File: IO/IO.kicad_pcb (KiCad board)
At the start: 2 copper layers, 100 x 100 mm, 36 parts, among them J1 Parallel, J2 Serial, J3 Buss, SW1 Slot, U1 74LS123, U2 74LS85, U3 MC6850, U4 MC6821, U5 74LS393, U6 74LS10, U7 74LS139, Y1 1.8432MHz

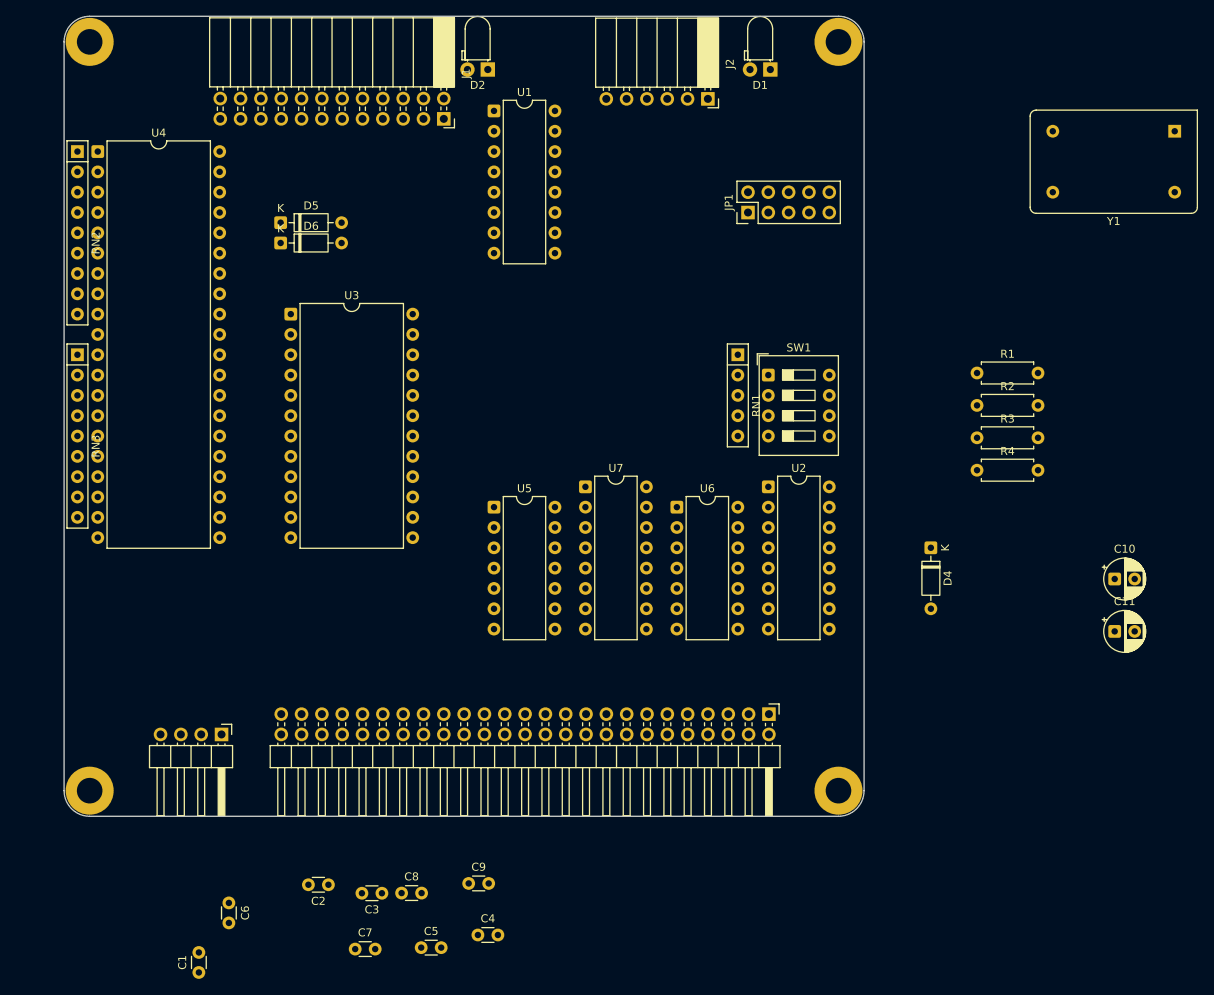
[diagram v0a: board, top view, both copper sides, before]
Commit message: finish routing the coms board. add some step models to look at this thing in freecad
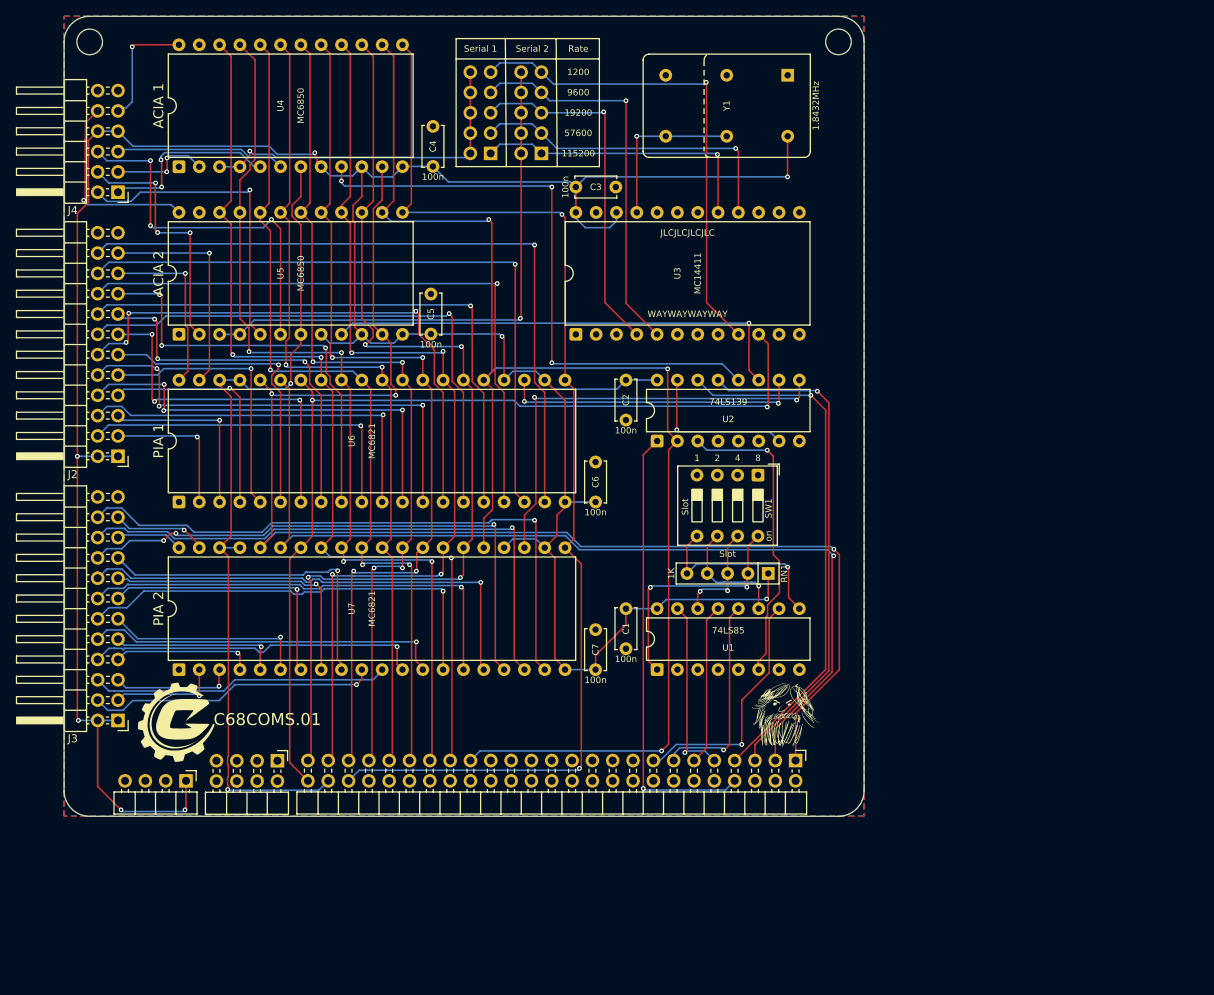
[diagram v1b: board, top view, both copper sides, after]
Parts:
- removed the C1 at (41.8, 144.5)
- removed C10, C11: 1µF, Capacitor_THT:CP_Radial_D5.0mm_P2.50mm
- removed C9: 100n, Capacitor_THT:C_Disc_D3.0mm_W1.6mm_P2.50mm
- removed D1: ACIA, LED_THT:LED_D3.0mm_Horizontal_O1.27mm_Z2.0mm
- removed D2: PIA, LED_THT:LED_D3.0mm_Horizontal_O1.27mm_Z2.0mm
- removed D4, D5, D6: 1N4148, Diode_THT:D_DO-35_SOD27_P7.62mm_Horizontal
- removed the J2 at (105.5, 35.3)
- removed R1, R2: 1K, Resistor_THT:R_Axial_DIN0207_L6.3mm_D2.5mm_P7.62mm_Horizontal
- removed R3, R4: 100K, Resistor_THT:R_Axial_DIN0207_L6.3mm_D2.5mm_P7.62mm_Horizontal
- removed RN2, RN3: 4.7K, Resistor_THT:R_Array_SIP9
- removed the U1 at (78.7, 36.8)
- removed the U6 at (101.6, 86.4)
- added G1: Logo, 0-Footprints:Crank, F.Cu at (39.1, 113.3)
- added G2: Logo, 0-Footprints:crankery_small, F.Cu at (114.9, 112.4)
- added J3: PIA 2, Connector_PinHeader_2.54mm:PinHeader_2x12_P2.54mm_Horizontal, F.Cu at (31.7, 113.0)
- added J4: Serial, Connector_PinHeader_2.54mm:PinHeader_2x06_P2.54mm_Horizontal, F.Cu at (31.7, 47.0)
- added JP2: RATE_{2}, 0-Footprints:PinHeader_2x05_P2.54mm_Vertical, F.Cu at (84.7, 42.1)
- added U3: MC14411, 0-Footprints:DIP-24_W15.24mm, F.Cu at (89.0, 64.8)
- added U7: MC6821, 0-Footprints:DIP-40_W15.24mm, F.Cu at (39.4, 106.7)
- C1: renamed from C2; footprint Capacitor_THT:C_Disc_D3.0mm_W1.6mm_P2.50mm -> 0-Footprints:C_Disc_D5.0mm_W2.5mm_P5.00mm
- C2: renamed from C7; footprint Capacitor_THT:C_Disc_D3.0mm_W1.6mm_P2.50mm -> 0-Footprints:C_Disc_D5.0mm_W2.5mm_P5.00mm
- C3, C4, C5, C6: footprint Capacitor_THT:C_Disc_D3.0mm_W1.6mm_P2.50mm -> 0-Footprints:C_Disc_D5.0mm_W2.5mm_P5.00mm
- C7: renamed from C8; footprint Capacitor_THT:C_Disc_D3.0mm_W1.6mm_P2.50mm -> 0-Footprints:C_Disc_D5.0mm_W2.5mm_P5.00mm
- J2: renamed from J1; value Parallel -> PIA 1; footprint Connector_PinSocket_2.54mm:PinSocket_2x12_P2.54mm_Horizontal -> Connector_PinHeader_2.54mm:PinHeader_2x12_P2.54mm_Horizontal
- JP1: value SERCLKx16 -> RATE_{1}; footprint Connector_PinHeader_2.54mm:PinHeader_2x05_P2.54mm_Vertical -> 0-Footprints:PinHeader_2x05_P2.54mm_Vertical
- RN1: footprint Resistor_THT:R_Array_SIP5 -> 0-Footprints:R_Array_SIP5
- SW1: footprint Button_Switch_THT:SW_DIP_SPSTx04_Slide_9.78x12.34mm_W7.62mm_P2.54mm -> 0-Footprints:SW_DIP_SPSTx04_Slide_9.78x12.34mm_W7.62mm_P2.54mm
- U1: renamed from U2; footprint Package_DIP:DIP-16_W7.62mm -> 0-Footprints:DIP-16_W7.62mm
- U2: renamed from U7; footprint Package_DIP:DIP-16_W7.62mm -> 0-Footprints:DIP-16_W7.62mm
- U4: renamed from U3; footprint Package_DIP:DIP-24_W15.24mm -> 0-Footprints:DIP-24_W15.24mm
- U5: value 74LS393 -> MC6850; footprint Package_DIP:DIP-14_W7.62mm -> 0-Footprints:DIP-24_W15.24mm
- U6: renamed from U4; footprint Package_DIP:DIP-40_W15.24mm -> 0-Footprints:DIP-40_W15.24mm
- Y1: footprint Oscillator:Oscillator_DIP-14 -> 0-Footprints:Oscillator_DIP-14
- moved C4 101.2 mm to (71.1, 38.8), turned to -90 degrees
- moved C3 93.0 mm to (94.0, 46.3)
- moved C5 81.7 mm to (70.9, 59.7), turned to -90 degrees
- moved C2 78.8 mm to (95.2, 70.5), turned to -90 degrees
- moved C6 71.7 mm to (91.4, 80.7)
- moved J2 58.6 mm to (31.7, 80.0), turned to 180 degrees
- moved C1 50.7 mm to (95.2, 99.0), turned to -90 degrees
- moved Y1 48.9 mm to (115.5, 32.4)
- moved U6 45.0 mm to (39.4, 85.7), turned to 90 degrees
- moved U5 44.9 mm to (39.4, 64.8), turned to 90 degrees
- moved C7 40.9 mm to (91.4, 101.7), turned to -90 degrees
- moved JP1 33.0 mm to (78.3, 42.1), turned to 180 degrees
- moved RN1 27.6 mm to (113.0, 94.7), turned to 180 degrees
- moved U1 26.7 mm to (99.1, 106.7), turned to 90 degrees
- moved U4 23.1 mm to (39.4, 43.8), turned to 90 degrees
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- renumbered J3 to J1
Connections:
- net Net-(J1-Pin_10) renamed /PB3
- net Net-(J1-Pin_11) renamed /PA4
- net Net-(J1-Pin_12) renamed /PB4
- net Net-(J1-Pin_13) renamed /PA5
- net Net-(J1-Pin_14) renamed /PB5
- net Net-(J1-Pin_15) renamed /PA6
- net Net-(J1-Pin_16) renamed /PB6
- net Net-(J1-Pin_17) renamed /PA7
- net Net-(J1-Pin_18) renamed /PB7
- net Net-(J1-Pin_19) renamed /CA1
- net Net-(J1-Pin_20) renamed /CB1
- net Net-(J1-Pin_21) renamed /CA2
- net Net-(J1-Pin_22) renamed /CB2
- net Net-(J1-Pin_3) renamed /PA0
- net Net-(J1-Pin_4) renamed /PB0
- net Net-(J1-Pin_5) renamed /PA1
- net Net-(J1-Pin_6) renamed /PB1
- net Net-(J1-Pin_7) renamed /PA2
- net Net-(J1-Pin_8) renamed /PB2
- net Net-(J1-Pin_9) renamed /PA3
- C3 pad 1: +5V -> GND
- C3 pad 2: GND -> +5V
- C4 pad 1: +5V -> GND
- C4 pad 2: GND -> +5V
- C5 pad 1: +5V -> GND
- C5 pad 2: GND -> +5V
- C6 pad 1: +5V -> GND
- C6 pad 2: GND -> +5V
- C7 pad 1: +5V -> GND
- C7 pad 2: GND -> +5V
- J1 pad 19: A9 -> unconnected-(J1-A_{9}-Pad19)
- J1 pad 21: A10 -> unconnected-(J1-A_{10}-Pad21)
- J1 pad 23: A11 -> unconnected-(J1-A_{11}-Pad23)
- J1 pad 25: A12 -> unconnected-(J1-A_{12}-Pad25)
- J1 pad 27: A13 -> unconnected-(J1-A_{13}-Pad27)
- J1 pad 29: A14 -> unconnected-(J1-A_{14}-Pad29)
- J1 pad 31: A15 -> unconnected-(J1-A_{15}-Pad31)
- J1 pad 48: Net-(D4-A) -> ~{IRQ}
- JP1 pad 1: /115200 -> 115.2Kbps
- JP1 pad 3: /57600 -> 57.6Kbps
- JP1 pad 5: /19200 -> 19.2Kbps
- JP1 pad 7: /9600 -> 9.6Kbps
- JP1 pad 9: /1200 -> 1.2Kbps
- U1 pad 6: Net-(U2-Oa=b) -> SLOT_SEL
- U2 pad 1: Net-(U7A-E) -> ~{IO_SEL}
- U2 pad 10: unconnected-(U7B-O2-Pad10) -> ~{PIA_{1}_SEL}
- U2 pad 11: unconnected-(U7B-O1-Pad11) -> ~{ACIA_{2}_SEL}
- U2 pad 12: unconnected-(U7B-O0-Pad12) -> ~{ACIA_{1}_SEL}
- U2 pad 13: GND -> A2
- U2 pad 14: GND -> A3
- U2 pad 15: GND -> Net-(U2A-O3)
- U2 pad 2: A3 -> BUS_OK
- U2 pad 3: GND -> SLOT_SEL
- U2 pad 4: ~{ACIA_SEL} -> unconnected-(U2A-O0-Pad4)
- U2 pad 5: ~{PIA_SEL} -> unconnected-(U2A-O1-Pad5)
- U2 pad 7: unconnected-(U7A-O3-Pad7) -> Net-(U2A-O3)
- U2 pad 9: unconnected-(U7B-O3-Pad9) -> ~{PIA_{2}_SEL}
- U4 pad 2: RXD -> RXD_{1}
- U4 pad 24: ~{CTS} -> ~{CTS_{1}}
- U4 pad 5: ~{RTS} -> ~{RTS_{1}}
- U4 pad 6: TXD -> TXD_{1}
- U4 pad 7: ~{IRQ_ACAI} -> ~{IRQ}
- U4 pad 9: ~{ACIA_SEL} -> ~{ACIA_{1}_SEL}
- U5 pad 1: /115200 -> GND
- U5 pad 10: /1200 -> +5V
- U5 pad 11: unconnected-(U5B-Q0-Pad11) -> A0
- U5 pad 12: GND -> +5V
- U5 pad 13: Net-(U5A-Q3) -> R/~{W}
- U5 pad 14: +5V -> BUS_OK
- U5 pad 2: GND -> RXD_{2}
- U5 pad 3: /57600 -> Net-(JP2-Pin_10)
- U5 pad 4: /19200 -> Net-(JP2-Pin_10)
- U5 pad 5: /9600 -> ~{RTS_{2}}
- U5 pad 6: Net-(U5A-Q3) -> TXD_{2}
- U5 pad 7: GND -> ~{IRQ}
- U5 pad 8: unconnected-(U5B-Q3-Pad8) -> +5V
- U5 pad 9: unconnected-(U5B-Q2-Pad9) -> ~{ACIA_{2}_SEL}
- U6 pad 23: ~{PIA_SEL} -> ~{PIA_{1}_SEL}
- U6 pad 37: ~{IRQB_PIA} -> ~{IRQ}
- U6 pad 38: ~{IRQA_PIA} -> ~{IRQ}
- Y1 pad 8: /115200 -> Net-(U3-X1)
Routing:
- net +5V: track 0.00 -> 373.1 mm, vias 0 -> 8
- net BUS_OK: track 0.00 -> 175.7 mm, vias 0 -> 3
- net A0: track 0.00 -> 170.2 mm, vias 0 -> 3
- net R/~{W}: track 0.00 -> 142.7 mm, vias 0 -> 2
- net D7: track 0.00 -> 123.9 mm, vias 0 -> 4
- net A1: track 0.00 -> 121.3 mm, vias 0 -> 1
- net ~{RESET}: track 0.00 -> 119.7 mm, vias 0 -> 2
- net D0: track 0.00 -> 118.7 mm, vias 0 -> 3
- net D6: track 0.00 -> 116.9 mm, vias 0 -> 4
- net D1: track 0.00 -> 114.6 mm, vias 0 -> 4
- net D5: track 0.00 -> 111.3 mm, vias 0 -> 4
- net D2: track 0.00 -> 108.4 mm, vias 0 -> 3
- net D4: track 0.00 -> 106.6 mm, vias 0 -> 4
- net ~{IRQ}: track 0.00 -> 106.2 mm, vias 0 -> 2
- net D3: track 0.00 -> 104.1 mm, vias 0 -> 2
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- added copper zone on B.Cu, net GND
- added copper zone on F.Cu, net GND
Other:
- board text added: "+5V"
- board text added: "1"
- board text added: "115200"
- board text added: "1200"
- board text added: "19200"
- board text added: "2"
- board text added: "3"
- board text added: "4"
- board text added: "57600"
- board text added: "8"
- board text added: "9600"
- board text added: "ACIA 1"
- board text added: "ACIA 2"
- board text added: "C1"
- board text added: "C2"
- board text added: "C68COMS.01"
- board text added: "Crankery - April 2026 - Dave Hamilton"
- board text added: "GND"
- board text added: "JLCJLCJLCJLC"
- board text added: "P0"
- board text added: "P1"
- board text added: "P2"
- board text added: "P3"
- board text added: "P4"
- board text added: "P5"
- board text added: "P6"
- board text added: "P7"
- board text added: "PIA 1"
- board text added: "PIA 2"
- board text added: "Parallel 1 & 2"
- board text added: "Parallel 3 & 4"
- board text added: "RXD"
- board text added: "Rate"
- board text added: "Serial 1"
- board text added: "Serial 1 & 2"
- board text added: "Serial 2"
- board text added: "Slot"
- board text added: "TXD"
- board text added: "WAYWAYWAYWAY"
- board text added: "~{CTS}"
- board text added: "~{RTS}"
